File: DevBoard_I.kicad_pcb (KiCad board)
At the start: 2 copper layers, 50.5 x 53 mm, 9 parts, among them J1 Barrel_Jack_Switch_Pin3Ring, U1 NCP1117-3.3_SOT223, U2 Arduino_UNO_R3, U3 AT25SF081-SSHD-X, U4 AT25SF081-SSHD-X, U5 MCP3550-60-ESN

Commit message: Rev_A Update
U5 footprint change.
Moved J1 and RV1 to the bottom.
Re-route accordingly.
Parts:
- J1, RV1: moved to B.Cu
- U5: footprint Package_SO:SOIC-8_3.9x4.9mm_P1.27mm -> Package_SO:MSOP-8_3x3mm_P0.65mm
- moved RV1 5.05 mm to (122.7, 52.5), turned to 180 degrees
- moved J1 0.15 mm to (125.5, 64.7), turned to 90 degrees
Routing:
- net Net-(C2-Pad1): track 132.1 -> 137.5 mm

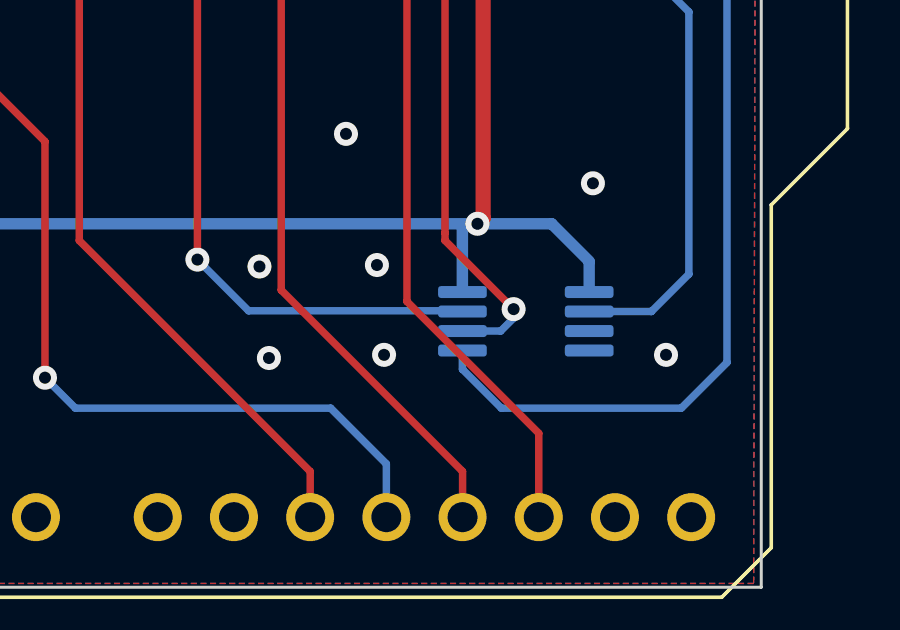
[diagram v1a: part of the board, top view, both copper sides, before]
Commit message: Added MCP3350 datasheet
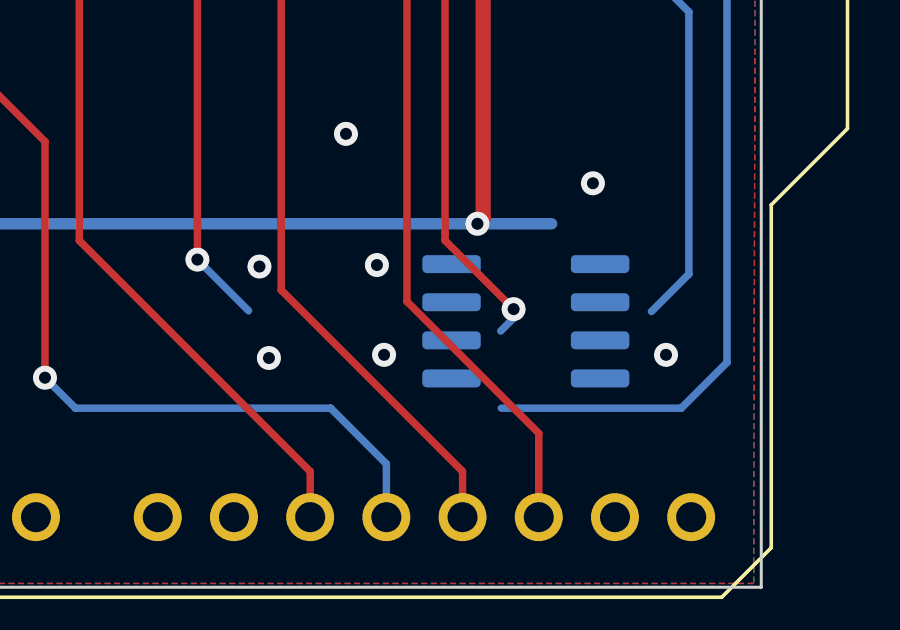
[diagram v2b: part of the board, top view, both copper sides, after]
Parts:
- U5: footprint Package_SO:MSOP-8_3x3mm_P0.65mm -> Package_SO:SOIC-8_3.9x4.9mm_P1.27mm
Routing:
- net Net-(U2-Pad9): track 50.8 -> 43.6 mm
- net Net-(C2-Pad1): track 137.5 -> 132.6 mm
- net /SCK: track 91.0 -> 88.5 mm
- net Net-(RV1-Pad2): track 75.6 -> 73.5 mm
- net /MISO: track 70.1 -> 68.9 mm

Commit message: N/A
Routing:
- net Net-(C2-Pad1): track 132.6 -> 142.1 mm
- net Net-(U2-Pad9): track 43.6 -> 50.3 mm
- net /MISO: track 68.9 -> 71.8 mm
- net Net-(U2-Pad18): track 48.4 -> 50.7 mm
- net /SCK: track 88.5 -> 90.6 mm
- net Net-(RV1-Pad2): track 73.5 -> 75.1 mm
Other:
- board text added: "JLCJLCJLCJLC"
- board text added: "REV B"
- board text removed: "REV A"
- board text removed: "W2023022600461049"
